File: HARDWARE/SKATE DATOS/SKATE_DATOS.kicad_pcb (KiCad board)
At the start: 2 copper layers, 8 parts, among them J1 MPU6050, J2 BMP280, J3 ENTRADA, SW1 INTERRUPTOR, U1 ESP32-DEVKIT-V1, U2 L7805

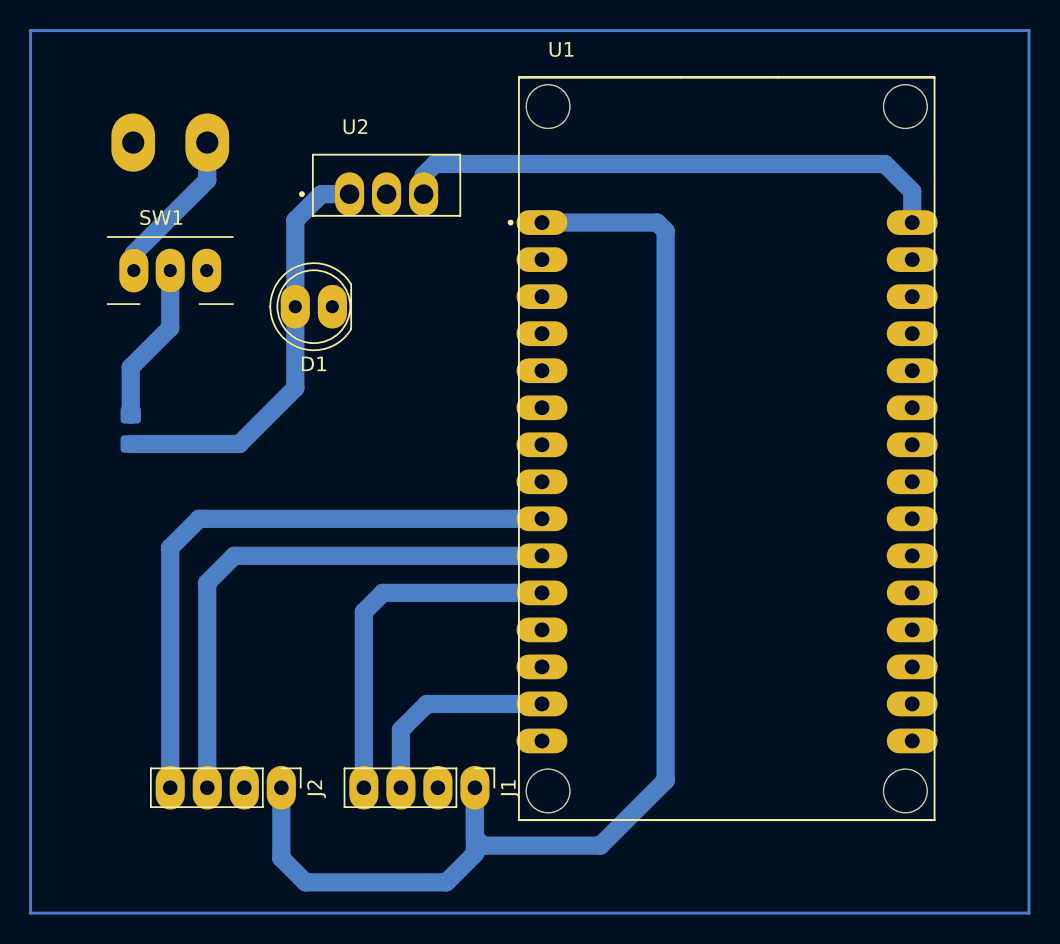
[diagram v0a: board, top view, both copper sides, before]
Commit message: capacitores de filtro
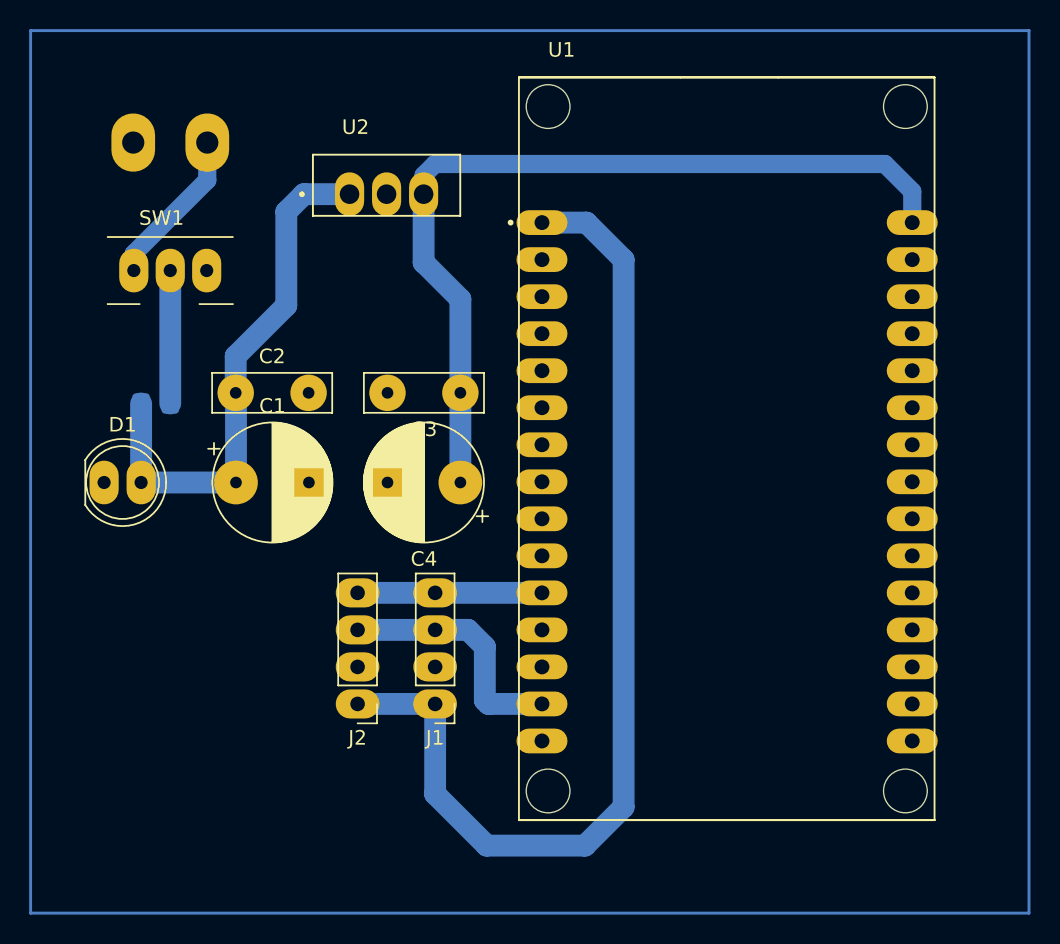
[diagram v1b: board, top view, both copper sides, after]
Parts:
- added C1: C_Polarized_US, Capacitor_THT:CP_Radial_D8.0mm_P5.00mm, F.Cu at (46.2, 47.8)
- added C2: C, Capacitor_THT:C_Disc_D8.0mm_W2.5mm_P5.00mm, F.Cu at (46.2, 41.7)
- added C3: C, Capacitor_THT:C_Disc_D8.0mm_W2.5mm_P5.00mm, F.Cu at (61.6, 41.7)
- added C4: C_Polarized_US, Capacitor_THT:CP_Radial_D8.0mm_P5.00mm, F.Cu at (61.6, 47.8)
- moved D1 19.8 mm to (37.1, 47.8), turned to 0 degrees
- moved J2 7.77 mm to (54.5, 63.0), turned to 180 degrees
- moved J1 6.37 mm to (59.9, 63.0), turned to 180 degrees
- moved R1 2.47 mm to (40.7, 42.4), turned to 180 degrees
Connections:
- J1 pad 3: SCL_MPU -> SCL_BMP
- J1 pad 4: SDA_MPU -> SDA_BMP
- U1 pad 10: SCL_BMP -> unconnected-(U1-D19-Pad10)
- U1 pad 11: SDA_MPU -> SDA_BMP
- U1 pad 14: SCL_MPU -> SCL_BMP
- U1 pad 9: SDA_BMP -> unconnected-(U1-D18-Pad9)
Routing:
- net SDA_BMP: track 42.8 -> 12.7 mm
- net SDA_MPU: track 24.8 -> 0.00 mm
- net SCL_BMP: track 37.8 -> 16.9 mm
- net +5V: track 38.1 -> 58.9 mm
- net +3.3V: track 89.1 -> 71.2 mm
- net SCL_MPU: track 14.4 -> 0.00 mm
- net Net-(D1-A): track 28.9 -> 36.8 mm
- net Net-(SW1-B): track 11.0 -> 9.12 mm
